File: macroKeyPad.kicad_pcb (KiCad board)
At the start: 2 copper layers, 102.3 x 39.6 mm, 18 parts, among them U1 kb2040

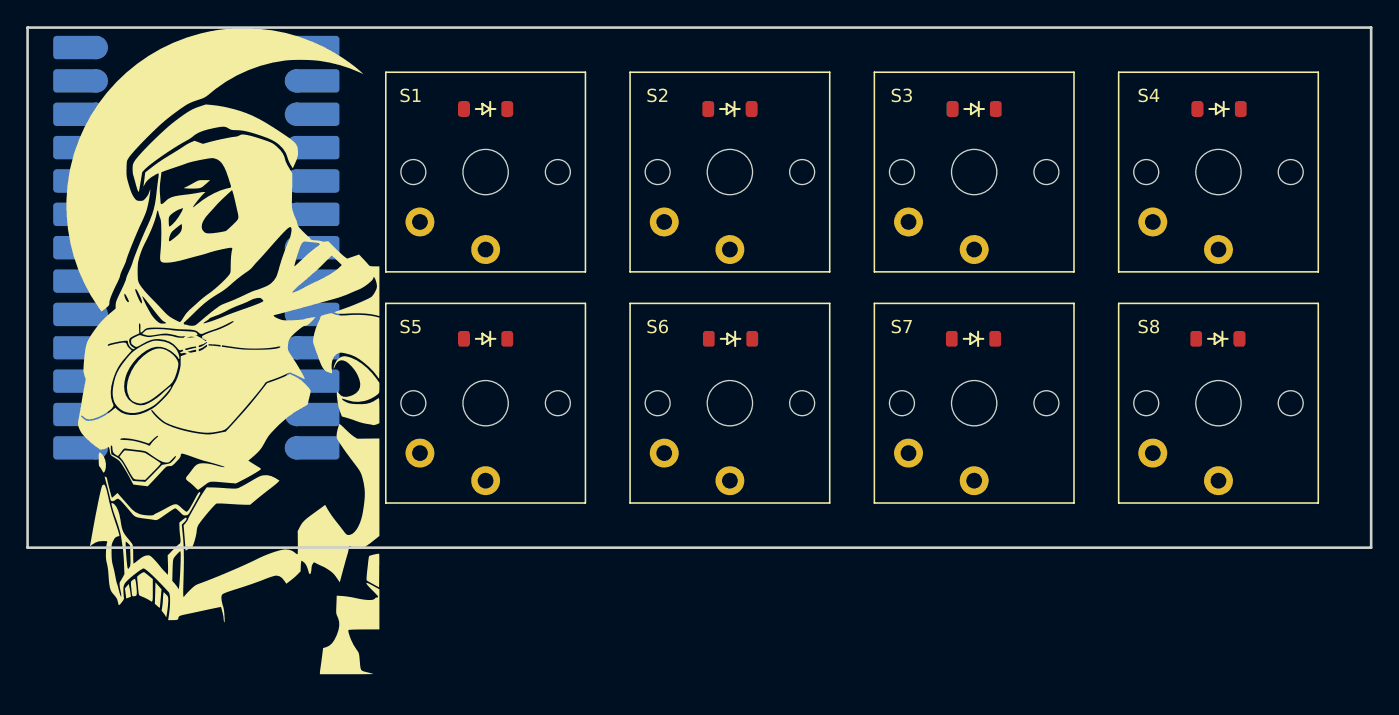
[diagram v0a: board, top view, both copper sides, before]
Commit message: added image and routes
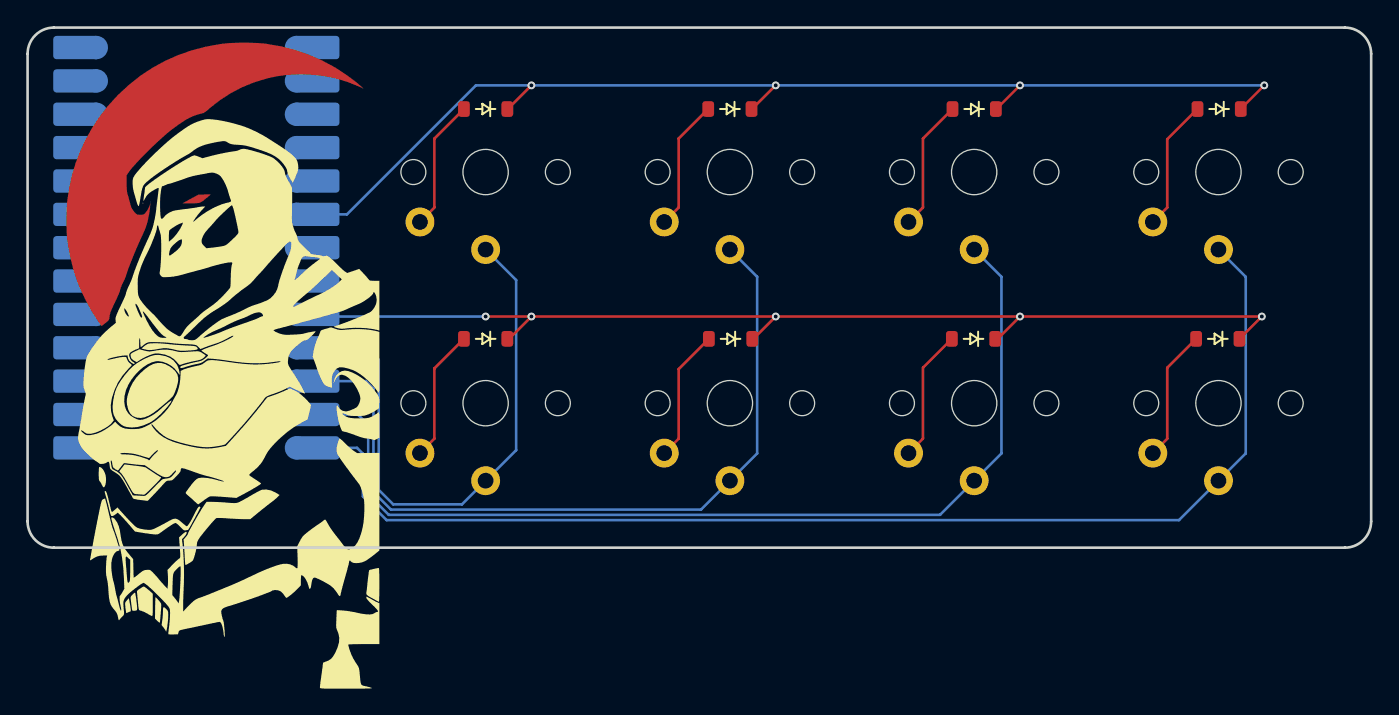
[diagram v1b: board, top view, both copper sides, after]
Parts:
- removed the G*** at (77.6, 66.0)
- added G*** (x2): LOGO, LOGO, F.Cu at (77.6, 67.1)
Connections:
- U1 pad 10: Col1 -> Col0
- U1 pad 11: Col0 -> Col1
- U1 pad 12: unconnected-(U1-D8-Pad12) -> Col2
- U1 pad 13: unconnected-(U1-D9-Pad13) -> Col3
- U1 pad 6: Row1 -> Row0
- U1 pad 7: Row0 -> unconnected-(U1-D3-Pad7)
- U1 pad 8: Col3 -> unconnected-(U1-D4-Pad8)
- U1 pad 9: Col2 -> Row1
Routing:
- net Col3: track 0.00 -> 93.4 mm
- net Row0: track 0.00 -> 86.5 mm, vias 0 -> 4
- net Row1: track 0.00 -> 82.1 mm, vias 0 -> 5
- net Col2: track 0.00 -> 76.8 mm
- net Col1: track 0.00 -> 60.4 mm
- net Col0: track 0.00 -> 43.9 mm
- net Net-(D6-A): track 0.00 -> 10.1 mm
- net Net-(D5-A): track 0.00 -> 10.1 mm
- net Net-(D7-A): track 0.00 -> 10.1 mm
- net Net-(D8-A): track 0.00 -> 10.1 mm
- net Net-(D4-A): track 0.00 -> 10.0 mm
- net Net-(D3-A): track 0.00 -> 9.99 mm
- net Net-(D2-A): track 0.00 -> 9.99 mm
- net Net-(D1-A): track 0.00 -> 9.99 mm
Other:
- outline, holes or cut-outs redrawn

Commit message: almost ready for production
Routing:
- net Row1: vias 5 -> 1
